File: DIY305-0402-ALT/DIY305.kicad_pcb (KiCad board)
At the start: 2 copper layers, 9.8 x 18.5 mm, 38 parts, among them J1 Conn_01x07, J2 Conn_01x07

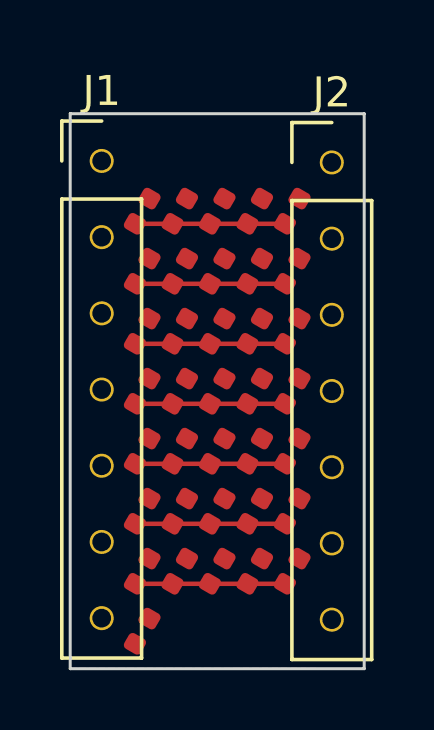
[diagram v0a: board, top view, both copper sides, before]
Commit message: finished up DIY-305-0402-ALT and fixed gitignore.
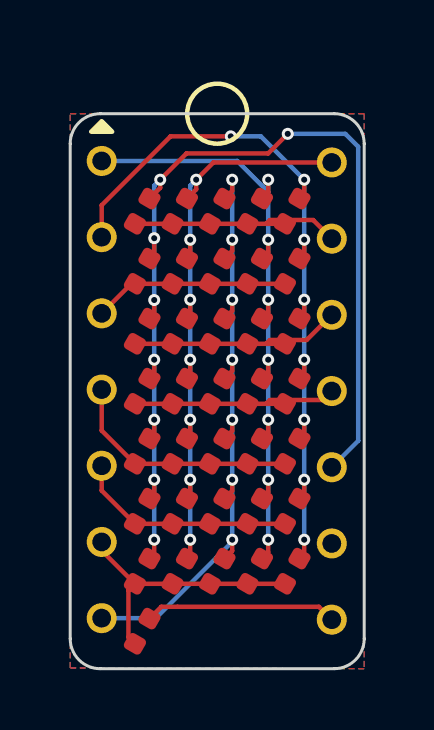
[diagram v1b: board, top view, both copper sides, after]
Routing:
- net C1: track 0.00 -> 35.5 mm, vias 0 -> 8
- net C5: track 0.00 -> 26.2 mm, vias 0 -> 8
- net C4: track 0.00 -> 23.0 mm, vias 0 -> 7
- net C3: track 0.00 -> 22.6 mm, vias 0 -> 7
- net C2: track 0.00 -> 21.6 mm, vias 0 -> 7
- net DP: track 0.00 -> 6.42 mm
- net R7: track 5.00 -> 9.03 mm
- net R5: track 5.00 -> 7.93 mm
- net R3: track 5.00 -> 7.59 mm
- net R1: track 5.00 -> 7.50 mm
- net R6: track 5.00 -> 7.39 mm
- net R4: track 5.00 -> 7.36 mm
- net R2: track 5.00 -> 6.52 mm
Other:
- outline, holes or cut-outs redrawn
- board text added: "env"
